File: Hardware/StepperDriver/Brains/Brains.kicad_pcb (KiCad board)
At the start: 2 copper layers, 102 x 81.3 mm, 14 parts, among them IC1 ATMEGA328-P, P1 CONN_01X02, P2 CONN_01X02, P3 CONN_01X07, P4 CONN_01X07, P5 CONN_01X07, P6 CONN_01X04, Y1 Crystal

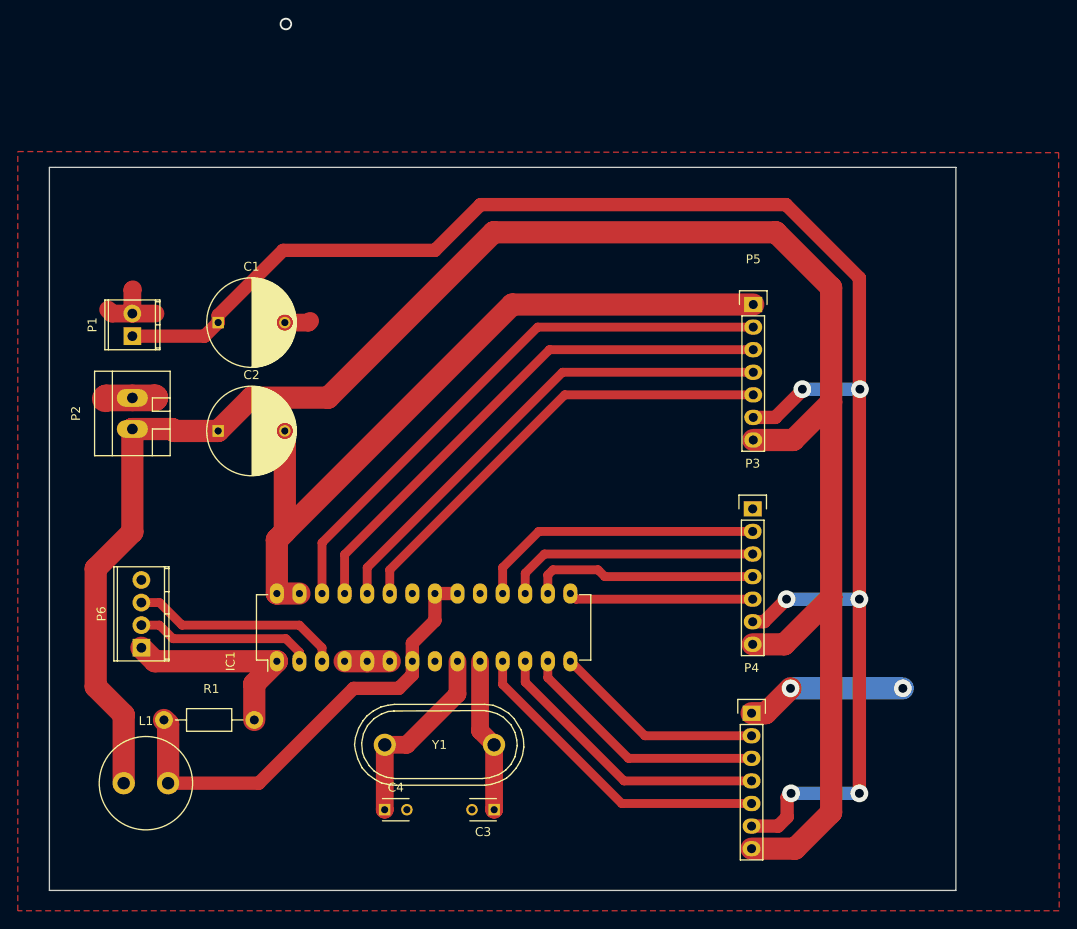
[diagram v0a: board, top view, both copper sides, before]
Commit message: various production tweaks: fixed track layers and footprints
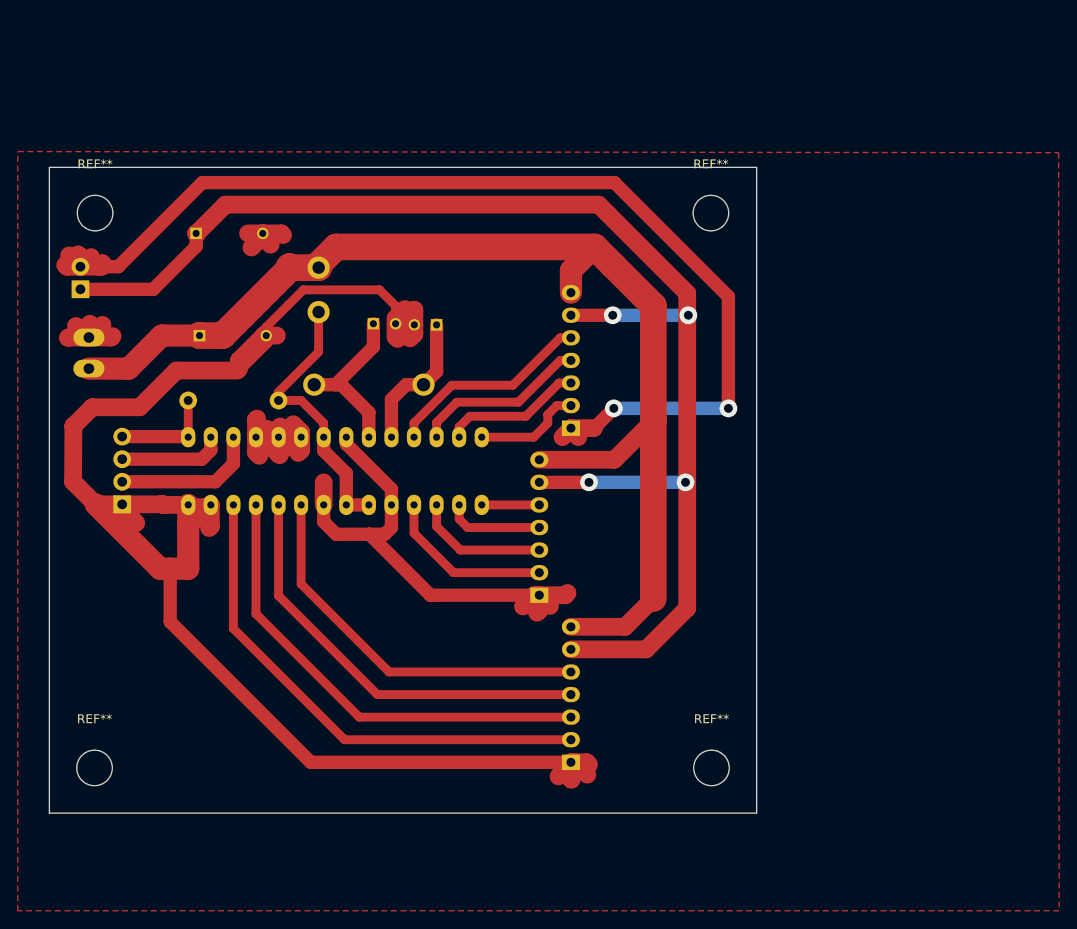
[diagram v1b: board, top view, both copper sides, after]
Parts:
- added REF**: MountingHole_4mm, Mounting_Holes:MountingHole_4mm, F.Cu at (133.1, 28.3)
- added REF**: MountingHole_4mm, Mounting_Holes:MountingHole_4mm, F.Cu at (133.2, 90.7)
- added REF**: MountingHole_4mm, Mounting_Holes:MountingHole_4mm, F.Cu at (63.8, 90.7)
- added REF**: MountingHole_4mm, Mounting_Holes:MountingHole_4mm, F.Cu at (63.8, 28.3)
- C1, C2, C3, C4, IC1, L1, P1, P2, P3, P4, P5, P6, R1, Y1: moved to B.Cu
- moved L1 58.8 mm to (89.0, 37.0), turned to 270 degrees
- moved P5 55.4 mm to (117.3, 90.1)
- moved C3 54.9 mm to (102.2, 40.9)
- moved C4 54.7 mm to (95.1, 40.8)
- moved Y1 41.3 mm to (94.6, 47.6)
- moved P4 38.0 mm to (117.3, 52.5)
- moved R1 36.0 mm to (79.4, 49.4), turned to 180 degrees
- moved IC1 27.1 mm to (74.3, 53.5), turned to 270 degrees
- moved P3 25.9 mm to (113.8, 71.3)
- moved P6 16.3 mm to (66.9, 61.1)
- moved C2 10.9 mm to (75.6, 42.1)
- moved C1 10.3 mm to (75.2, 30.6)
- moved P2 8.37 mm to (63.1, 44.1)
- moved P1 7.87 mm to (62.2, 36.9)
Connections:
- P6 pad 1: Net-(IC1-Pad1) -> GND
- P6 pad 2: Net-(IC1-Pad2) -> Net-(IC1-Pad3)
- P6 pad 3: Net-(IC1-Pad3) -> Net-(IC1-Pad2)
- P6 pad 4: GND -> Net-(IC1-Pad1)
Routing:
- net GND: track 125.9 -> 404.9 mm
- net +5V: track 224.7 -> 136.9 mm
- net +9V: track 191.4 -> 158.4 mm, vias 6 -> 4
- net Net-(IC1-Pad3): track 45.9 -> 16.3 mm
- net Net-(IC1-Pad2): track 38.1 -> 11.9 mm
- net +5VD: track 53.2 -> 30.7 mm
- net Net-(IC1-Pad1): track 33.3 -> 11.6 mm
- net /STEPPER1PHASEA2: track 25.7 -> 11.0 mm
- net /STEPPER1PHASEA1: track 20.8 -> 6.92 mm
- net /STEPPER1PHASEB1: track 28.8 -> 15.1 mm
- net /STEPPER1PHASEB2: track 32.7 -> 19.1 mm
- net /STEPPER2PHASEA1: track 36.2 -> 23.2 mm
- net /STEPPER2PHASEA2: track 32.4 -> 19.7 mm
- net /STEPPER2PHASEB2: track 23.9 -> 12.1 mm
- net /STEPPER2PHASEB1: track 28.5 -> 16.9 mm
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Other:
- board size 102 x 81.3 mm -> 79.6 x 72.6 mm
- net class Default: trace_width 0.5 -> 1
- net class data: trace_width 0.5 -> 1
